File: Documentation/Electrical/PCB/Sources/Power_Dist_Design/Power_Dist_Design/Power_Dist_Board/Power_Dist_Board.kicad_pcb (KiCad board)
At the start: 2 copper layers, 175 x 97.5 mm, 47 parts, among them J1 Battery Connector, J2 5V Connector, J3 3.3V Connector, M1 Motor_DC, M2 Motor_DC, M3 Motor_DC, M4 Motor_DC, M5 Motor_DC, M6 Motor_DC, SW1 Emergency Stop, U1 TPS565201, U2 TPS565201

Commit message: Made further edits to pcb
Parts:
- added J4: +3.3V, Power_Dist:Pwr_Rail_Conn_Custom, F.Cu at (157.8, 88.0)
- added J5: +3.3V, Power_Dist:Pwr_Rail_Conn_Custom, F.Cu at (171.7, 41.0)
- added J6: GND, Power_Dist:Pwr_Rail_Conn_Custom, F.Cu at (157.8, 94.0)
- added J7: GND, Power_Dist:Pwr_Rail_Conn_Custom, F.Cu at (171.7, 35.0)
- D1: value LED -> LED1
- D2: value LED -> LED2
- D3: value LED -> LED3
- J2: value 5V Connector -> +5V; footprint Connector_Phoenix_MSTB:PhoenixContact_MSTBVA_2,5_2-G-5,08_1x02_P5.08mm_Vertical -> Power_Dist:Pwr_Rail_Conn_Custom
- J3: value 3.3V Connector -> +5V; footprint Connector_Phoenix_MSTB:PhoenixContact_MSTBVA_2,5_2-G-5,08_1x02_P5.08mm_Vertical -> Power_Dist:Pwr_Rail_Conn_Custom
- moved J3 82.5 mm to (171.7, 29.0), turned to -90 degrees
- moved SW1 77.9 mm to (92.0, 40.0), turned to -90 degrees
- moved D3 62.4 mm to (98.8, 36.0), turned to 90 degrees
- moved R3 52.8 mm to (98.8, 29.2), turned to -90 degrees
- moved J1 50.6 mm to (92.0, 29.0), turned to -90 degrees
- moved F3 50.2 mm to (104.8, 33.8), turned to -90 degrees
- moved J2 21.7 mm to (157.8, 100.0), turned to -90 degrees
- moved F2 12.1 mm to (111.3, 62.7), turned to 0 degrees
- moved F1 12.0 mm to (162.5, 63.0), turned to 0 degrees
- moved D2 8.46 mm to (116.0, 69.0), turned to -90 degrees
- moved R2 8.06 mm to (119.2, 69.0)
- moved R1 7.52 mm to (171.0, 69.5)
- moved D1 7.38 mm to (167.0, 69.5), turned to -90 degrees
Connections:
- J3 pad 1: +3.3V -> +5V
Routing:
- net +12V: track 272.2 -> 316.2 mm
- net /vin: track 151.1 -> 109.9 mm, vias 4 -> 7
- net +3.3V: track 34.4 -> 8.22 mm
- net +5V: track 34.5 -> 14.1 mm, vias 0 -> 2
- net GND: track 167.8 -> 187.8 mm, vias 0 -> 14
- net /vout2: track 50.2 -> 41.3 mm
- net /vout1: track 48.5 -> 44.3 mm
- net Net-(D3-Pad2): track 5.96 -> 3.78 mm
- net Net-(D3-Pad1): track 20.3 -> 18.7 mm
- added copper zone on F.Cu, net +3.3V
- added copper zone on B.Cu, net +5V
- added copper zone on F.Cu, net +5V
- added copper zone on B.Cu, net GND
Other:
- board size 175 x 97.5 mm -> 150.5 x 84.8 mm
- board text added: "+ -"
- board text added: "LED1 - 5V Rail Fuse LED2 - 3.3V Rail Fuse LED3 - 12V Rail Fuse"
- board text added: "Motors"
- board text added: "Output"
- board text removed: "+"
- board text removed: "+3.3V"
- board text removed: "+5V"
- board text removed: "-"
- board text removed: "GND"

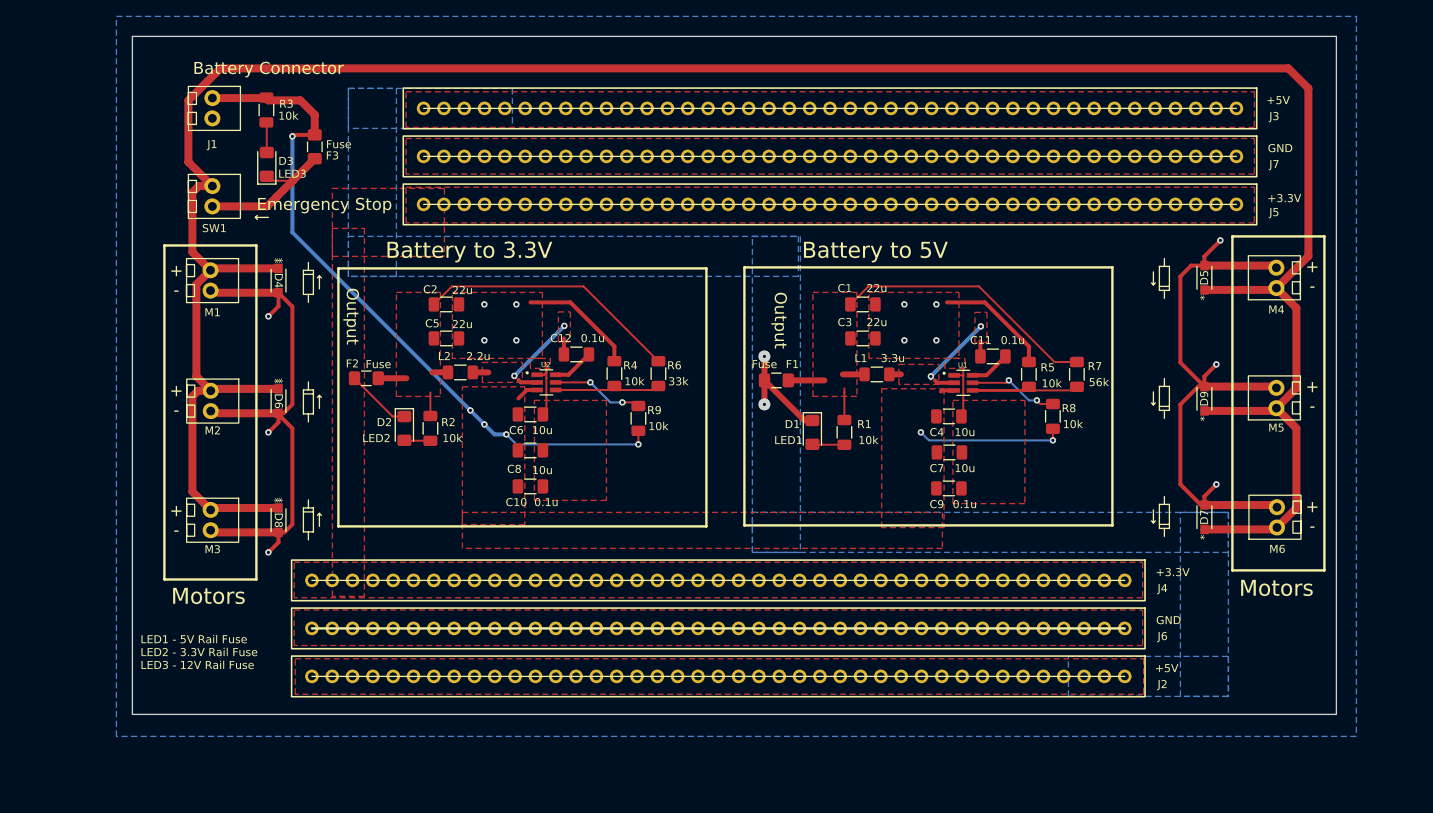
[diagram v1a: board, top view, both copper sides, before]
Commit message: Increased width of 12V rail traces
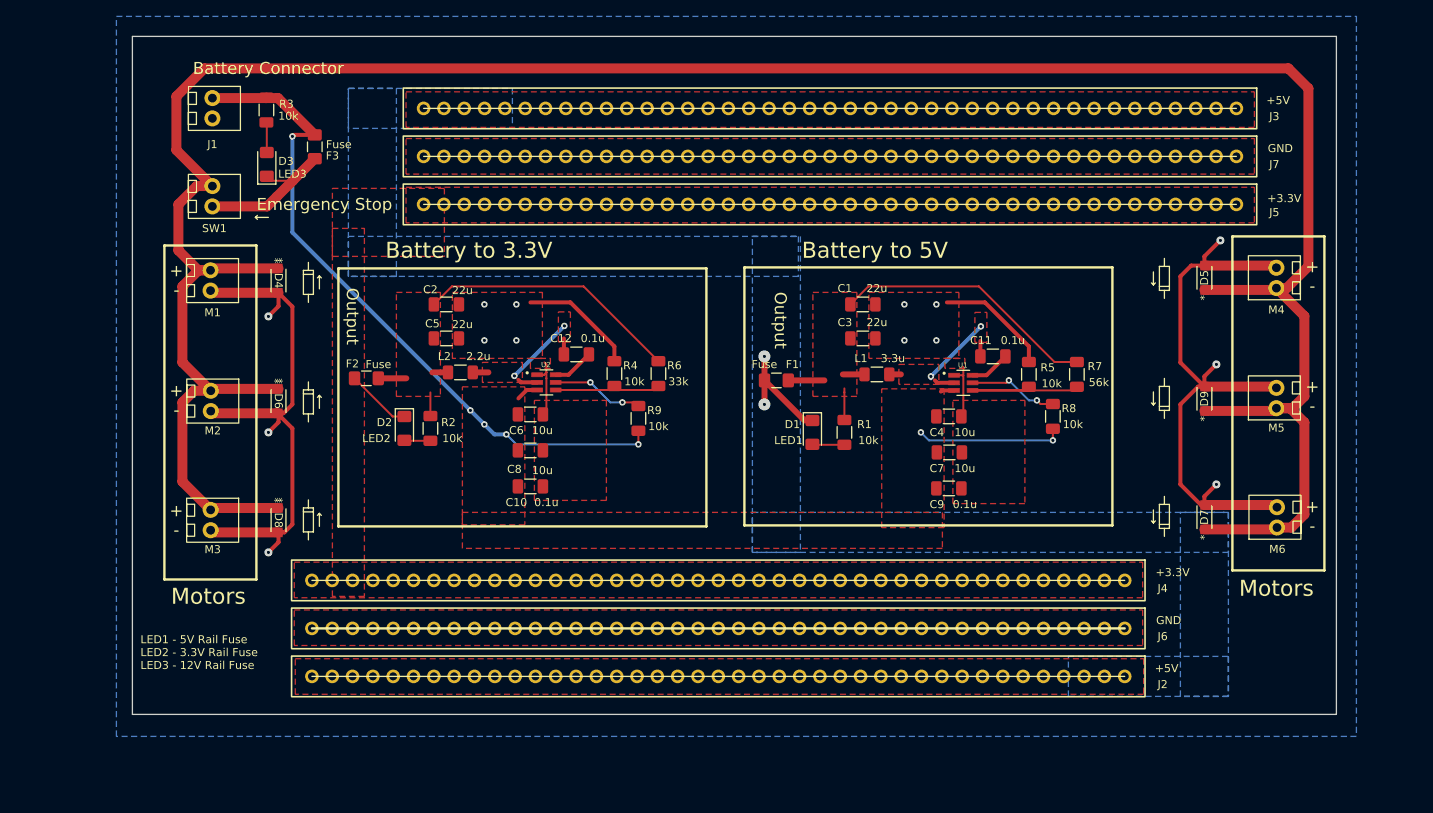
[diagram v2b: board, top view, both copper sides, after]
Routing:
- net +12V: track 316.2 -> 330.4 mm
- net /vin: track 109.9 -> 108.4 mm

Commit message: Added more motor terminals
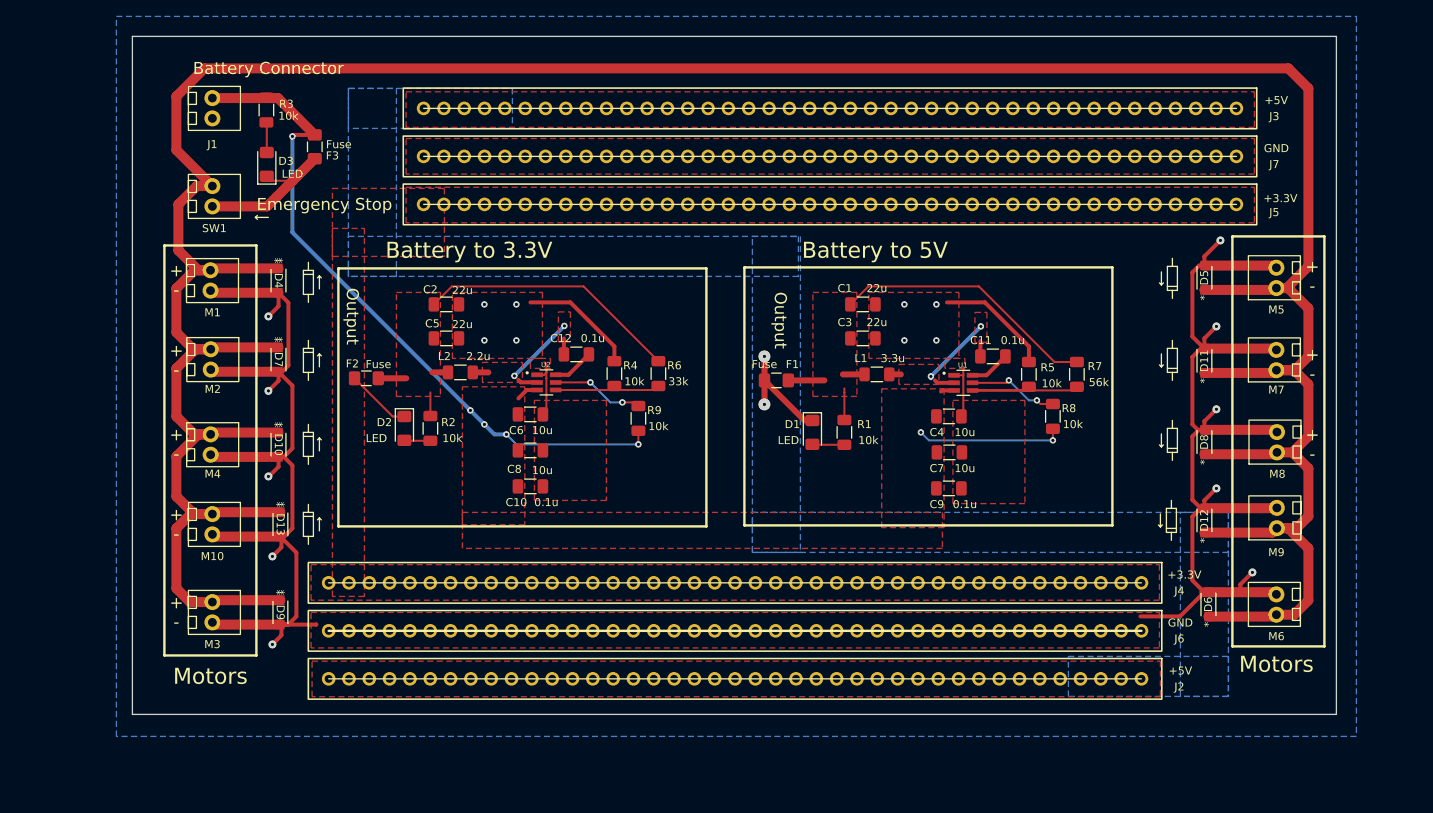
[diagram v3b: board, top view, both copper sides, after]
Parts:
- added D12: D, RB070MM:DIO_RB051MM_ROM-M, F.Cu at (216.0, 80.5)
- added D13: D, RB070MM:DIO_RB051MM_ROM-M, F.Cu at (100.5, 81.0)
- added D6: D, RB070MM:DIO_RB051MM_ROM-M, F.Cu at (216.5, 91.0)
- added D9: D, RB070MM:DIO_RB051MM_ROM-M, F.Cu at (100.5, 92.0)
- added M10: Motor_DC, Power_Dist:Molex_Screw_Term_0397730002, F.Cu at (92.0, 81.0)
- added M3: Motor_DC, Power_Dist:Molex_Screw_Term_0397730002, F.Cu at (92.0, 92.0)
- added M6: Motor_DC, Power_Dist:Molex_Screw_Term_0397730002, F.Cu at (225.0, 91.0)
- added M9: Motor_DC, Power_Dist:Molex_Screw_Term_0397730002, F.Cu at (225.1, 80.2)
- D1: value LED1 -> LED
- D2: value LED2 -> LED
- D3: value LED3 -> LED
- moved D10 9.44 mm to (100.3, 71.0)
- moved M4 9.44 mm to (91.8, 71.0)
- moved D8 9.39 mm to (216.0, 70.7)
- moved M8 9.39 mm to (225.1, 70.7)
- moved D7 5.19 mm to (100.3, 60.4)
- moved M2 5.19 mm to (91.8, 60.4)
- moved D11 4.75 mm to (216.0, 60.5)
- moved M7 4.75 mm to (225.0, 60.4)
- moved J2 2.12 mm to (159.9, 100.3)
- moved J4 2.12 mm to (159.9, 88.3)
- moved J6 2.12 mm to (159.9, 94.3)
- renumbered D8 to D10, D9 to D11, D6 to D7, D7 to D8, M3 to M4, M4 to M5, M5 to M7, M6 to M8
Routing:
- net GND: track 187.8 -> 273.5 mm, vias 14 -> 18
- net +12V: track 330.4 -> 416.2 mm
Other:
- board text removed: "LED1 - 5V Rail Fuse LED2 - 3.3V Rail Fuse LED3 - 12V Rail Fuse"
